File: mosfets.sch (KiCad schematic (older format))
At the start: 28 parts, among them Q12 PSMN1R2-30YLC,115, Q13 PSMN1R2-30YLC,115, Q14 PSMN1R2-30YLC,115, Q15 IRLML0030TRPbF, Q16 IRLML0030TRPbF, Q17 IRLML0030TRPbF, Q18 IRLML0030TRPbF

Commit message: Improve Readability
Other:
- moved on the sheet: D10, D11, D12, D13, D7, D8, D9, R39, R43
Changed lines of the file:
@@
 L Device:D_Schottky D7
 U 1 1 5B1A3271
-P 1950 1300
-F 0 "D7" H 1950 1516 50  0000 C CNN
-F 1 "SK310A-LTP" H 1950 1425 50  0000 C CNN
-F 2 "Diode_SMD:D_SMA" H 1950 1300 50  0001 C CNN
-F 3 "https://www.mouser.de/ProductDetail/Micro-Commercial-Components-MCC/SK310A-TP?qs=O2qRfqcg9D9SKx4%252bV6P4XQ%3D%3D" H 1950 1300 50  0001 C CNN
-	1    1950 1300
-	1    0    0    -1
-$EndComp
-Wire Wire Line
-	1700 1300 1800 1300
+P 2000 1300
+F 0 "D7" H 2000 1516 50  0000 C CNN
+F 1 "SK310A-LTP" H 2000 1425 50  0000 C CNN
+F 2 "Diode_SMD:D_SMA" H 2000 1300 50  0001 C CNN
+F 3 "https://www.mouser.de/ProductDetail/Micro-Commercial-Components-MCC/SK310A-TP?qs=O2qRfqcg9D9SKx4%252bV6P4XQ%3D%3D" H 2000 1300 50  0001 C CNN
+	1    2000 1300
+	1    0    0    -1
+$EndComp
+Wire Wire Line
+	1700 1300 1850 1300
 $Comp
 L heteromycin:PSMN1R8-40YLC,115 Q12
@@
 L Device:D_Schottky D8
 U 1 1 5B1B03B6
-P 1950 2950
-F 0 "D8" H 1950 3166 50  0000 C CNN
-F 1 "SK310A-LTP" H 1950 3075 50  0000 C CNN
-F 2 "Diode_SMD:D_SMA" H 1950 2950 50  0001 C CNN
-F 3 "https://www.mouser.de/ProductDetail/Micro-Commercial-Components-MCC/SK310A-TP?qs=O2qRfqcg9D9SKx4%252bV6P4XQ%3D%3D" H 1950 2950 50  0001 C CNN
-	1    1950 2950
-	1    0    0    -1
-$EndComp
-Wire Wire Line
-	1700 2950 1800 2950
+P 2000 2950
+F 0 "D8" H 2000 3166 50  0000 C CNN
+F 1 "SK310A-LTP" H 2000 3075 50  0000 C CNN
+F 2 "Diode_SMD:D_SMA" H 2000 2950 50  0001 C CNN
+F 3 "https://www.mouser.de/ProductDetail/Micro-Commercial-Components-MCC/SK310A-TP?qs=O2qRfqcg9D9SKx4%252bV6P4XQ%3D%3D" H 2000 2950 50  0001 C CNN
+	1    2000 2950
+	1    0    0    -1
+$EndComp
+Wire Wire Line
+	1700 2950 1850 2950
 Wire Wire Line
 	2400 3850 2500 3850
@@
 	2300 3200 2300 2950
 Wire Wire Line
-	2300 2950 2100 2950
-Wire Wire Line
-	2100 1300 2300 1300
+	2300 2950 2150 2950
+Wire Wire Line
+	2150 1300 2300 1300
 Connection ~ 2300 1300
 Wire Wire Line
@@
 	4900 1750 5000 1750
 Wire Wire Line
-	5250 1300 5350 1300
-Wire Wire Line
-	5650 1300 5850 1300
+	5250 1300 5400 1300
+Wire Wire Line
+	5700 1300 5850 1300
 Connection ~ 5850 1300
 Wire Wire Line
@@
 L Device:R R39
 U 1 1 5B2008D0
-P 5150 3400
-F 0 "R39" V 4943 3400 50  0000 C CNN
-F 1 "100" V 5034 3400 50  0000 C CNN
-F 2 "Resistor_SMD:R_0603_1608Metric" V 5080 3400 50  0001 C CNN
-F 3 "~" H 5150 3400 50  0001 C CNN
-	1    5150 3400
-	0    1    1    0
-$EndComp
-Text HLabel 4900 3400 0    50   Input ~ 0
+P 5200 3400
+F 0 "R39" V 4993 3400 50  0000 C CNN
+F 1 "100" V 5084 3400 50  0000 C CNN
+F 2 "Resistor_SMD:R_0603_1608Metric" V 5130 3400 50  0001 C CNN
+F 3 "~" H 5200 3400 50  0001 C CNN
+	1    5200 3400
+	0    1    1    0
+$EndComp
+Text HLabel 4950 3400 0    50   Input ~ 0
 PWM_FAN3
 Wire Wire Line
-	4900 3400 5000 3400
-Wire Wire Line
-	5250 2950 5350 2950
-Wire Wire Line
-	5650 2950 5850 2950
+	4950 3400 5050 3400
+Wire Wire Line
+	5250 2950 5400 2950
+Wire Wire Line
+	5700 2950 5850 2950
 Connection ~ 5850 2950
 Wire Wire Line
@@
 Wire Wire Line
 	5350 1750 5550 1750
-Wire Wire Line
-	1650 1750 1800 1750
-Wire Wire Line
-	1650 3400 1800 3400
 $Comp
 L Device:R R35
@@
 	2300 2200 2100 2200
 Connection ~ 2300 2200
-Wire Wire Line
-	1800 2200 1800 1750
-Connection ~ 1800 1750
-Wire Wire Line
-	1800 1750 2000 1750
 $Comp
 L Device:R R36
@@
 Wire Wire Line
 	5400 3850 5500 3850
-Wire Wire Line
-	5300 3400 5400 3400
 Connection ~ 5400 3400
 Wire Wire Line
@@
 	5850 3850 5800 3850
 Connection ~ 5850 3850
-Wire Wire Line
-	1800 3850 1800 3400
-Connection ~ 1800 3400
-Wire Wire Line
-	1800 3400 2000 3400
 Text GLabel 5250 1300 0    50   Input ~ 0
 VDD_FAN
@@
 L Device:D_Schottky D10
 U 1 1 5BD6B250
-P 5500 1300
-F 0 "D10" H 5450 1500 50  0000 L CNN
-F 1 "BAT54GWJ" H 5300 1400 50  0000 L CNN
-F 2 "Diode_SMD:D_SOD-123" H 5500 1300 50  0001 C CNN
-F 3 "https://www.mouser.de/datasheet/2/916/BAT54GW-1318921.pdf" H 5500 1300 50  0001 C CNN
-	1    5500 1300
+P 5550 1300
+F 0 "D10" H 5500 1500 50  0000 L CNN
+F 1 "BAT54GWJ" H 5350 1400 50  0000 L CNN
+F 2 "Diode_SMD:D_SOD-123" H 5550 1300 50  0001 C CNN
+F 3 "https://www.mouser.de/datasheet/2/916/BAT54GW-1318921.pdf" H 5550 1300 50  0001 C CNN
+	1    5550 1300
 	1    0    0    -1
 $EndComp
@@
 L Device:D_Schottky D11
 U 1 1 5BD6D4A2
-P 5500 2950
-F 0 "D11" H 5450 3150 50  0000 L CNN
-F 1 "BAT54GWJ" H 5300 3050 50  0000 L CNN
-F 2 "Diode_SMD:D_SOD-123" H 5500 2950 50  0001 C CNN
-F 3 "https://www.mouser.de/datasheet/2/916/BAT54GW-1318921.pdf" H 5500 2950 50  0001 C CNN
-	1    5500 2950
+P 5550 2950
+F 0 "D11" H 5500 3150 50  0000 L CNN
+F 1 "BAT54GWJ" H 5350 3050 50  0000 L CNN
+F 2 "Diode_SMD:D_SOD-123" H 5550 2950 50  0001 C CNN
+F 3 "https://www.mouser.de/datasheet/2/916/BAT54GW-1318921.pdf" H 5550 2950 50  0001 C CNN
+	1    5550 2950
 	1    0    0    -1
 $EndComp
@@
 L Device:D_Schottky D9
 U 1 1 5BC4CDE5
-P 1950 4450
-F 0 "D9" H 1950 4666 50  0000 C CNN
-F 1 "SK310A-LTP" H 1950 4575 50  0000 C CNN
-F 2 "Diode_SMD:D_SMA" H 1950 4450 50  0001 C CNN
-F 3 "https://www.mouser.de/ProductDetail/Micro-Commercial-Components-MCC/SK310A-TP?qs=O2qRfqcg9D9SKx4%252bV6P4XQ%3D%3D" H 1950 4450 50  0001 C CNN
-	1    1950 4450
-	1    0    0    -1
-$EndComp
-Wire Wire Line
-	1700 4450 1800 4450
+P 2000 4450
+F 0 "D9" H 2000 4666 50  0000 C CNN
+F 1 "SK310A-LTP" H 2000 4575 50  0000 C CNN
+F 2 "Diode_SMD:D_SMA" H 2000 4450 50  0001 C CNN
+F 3 "https://www.mouser.de/ProductDetail/Micro-Commercial-Components-MCC/SK310A-TP?qs=O2qRfqcg9D9SKx4%252bV6P4XQ%3D%3D" H 2000 4450 50  0001 C CNN
+	1    2000 4450
+	1    0    0    -1
+$EndComp
+Wire Wire Line
+	1700 4450 1850 4450
 Wire Wire Line
 	2400 5350 2500 5350
@@
 	2300 4700 2300 4450
 Wire Wire Line
-	2300 4450 2100 4450
+	2300 4450 2150 4450
 Wire Wire Line
 	2600 4450 2300 4450
 Connection ~ 2300 4450
-Wire Wire Line
-	1650 4900 1800 4900
 $Comp
 L Device:R R37
@@
 Wire Wire Line
 	2300 5350 2100 5350
-Wire Wire Line
-	1800 5350 1800 4900
-Connection ~ 1800 4900
-Wire Wire Line
-	1800 4900 2000 4900
 $Comp
 L heteromycin:PSMN1R8-40YLC,115 Q14
@@
 	7350 1750 7450 1750
 Wire Wire Line
-	7700 1300 7800 1300
-Wire Wire Line
-	8100 1300 8300 1300
+	7700 1300 7850 1300
+Wire Wire Line
+	8150 1300 8300 1300
 Connection ~ 8300 1300
 Wire Wire Line
@@
 L Device:R R43
 U 1 1 5BC57CE1
-P 7600 3400
-F 0 "R43" V 7393 3400 50  0000 C CNN
-F 1 "100" V 7484 3400 50  0000 C CNN
-F 2 "Resistor_SMD:R_0603_1608Metric" V 7530 3400 50  0001 C CNN
-F 3 "~" H 7600 3400 50  0001 C CNN
-	1    7600 3400
-	0    1    1    0
-$EndComp
-Text HLabel 7350 3400 0    50   Input ~ 0
+P 7650 3400
+F 0 "R43" V 7443 3400 50  0000 C CNN
+F 1 "100" V 7534 3400 50  0000 C CNN
+F 2 "Resistor_SMD:R_0603_1608Metric" V 7580 3400 50  0001 C CNN
+F 3 "~" H 7650 3400 50  0001 C CNN
+	1    7650 3400
+	0    1    1    0
+$EndComp
+Text HLabel 7400 3400 0    50   Input ~ 0
 PWM_FAN4
 Wire Wire Line
-	7350 3400 7450 3400
-Wire Wire Line
-	7700 2950 7800 2950
-Wire Wire Line
-	8100 2950 8300 2950
+	7400 3400 7500 3400
+Wire Wire Line
+	7700 2950 7850 2950
+Wire Wire Line
+	8150 2950 8300 2950
 Connection ~ 8300 2950
 Wire Wire Line
@@
 	7850 3850 7950 3850
 Wire Wire Line
-	7750 3400 7850 3400
+	7800 3400 7850 3400
 Connection ~ 7850 3400
-Wire Wire Line
-	7850 3400 8000 3400
 Wire Wire Line
 	8300 3850 8250 3850
@@
 L Device:D_Schottky D12
 U 1 1 5BC57D0F
-P 7950 1300
-F 0 "D12" H 7900 1500 50  0000 L CNN
-F 1 "BAT54GWJ" H 7750 1400 50  0000 L CNN
-F 2 "Diode_SMD:D_SOD-123" H 7950 1300 50  0001 C CNN
-F 3 "https://www.mouser.de/datasheet/2/916/BAT54GW-1318921.pdf" H 7950 1300 50  0001 C CNN
-	1    7950 1300
+P 8000 1300
+F 0 "D12" H 7950 1500 50  0000 L CNN
+F 1 "BAT54GWJ" H 7800 1400 50  0000 L CNN
+F 2 "Diode_SMD:D_SOD-123" H 8000 1300 50  0001 C CNN
+F 3 "https://www.mouser.de/datasheet/2/916/BAT54GW-1318921.pdf" H 8000 1300 50  0001 C CNN
+	1    8000 1300
 	1    0    0    -1
 $EndComp
@@
 L Device:D_Schottky D13
 U 1 1 5BC57D16
-P 7950 2950
-F 0 "D13" H 7900 3150 50  0000 L CNN
-F 1 "BAT54GWJ" H 7750 3050 50  0000 L CNN
-F 2 "Diode_SMD:D_SOD-123" H 7950 2950 50  0001 C CNN
-F 3 "https://www.mouser.de/datasheet/2/916/BAT54GW-1318921.pdf" H 7950 2950 50  0001 C CNN
-	1    7950 2950
+P 8000 2950
+F 0 "D13" H 7950 3150 50  0000 L CNN
+F 1 "BAT54GWJ" H 7800 3050 50  0000 L CNN
+F 2 "Diode_SMD:D_SOD-123" H 8000 2950 50  0001 C CNN
+F 3 "https://www.mouser.de/datasheet/2/916/BAT54GW-1318921.pdf" H 8000 2950 50  0001 C CNN
+	1    8000 2950
 	1    0    0    -1
 $EndComp
@@
 	1    0    0    -1
 $EndComp
+Wire Wire Line
+	7850 3400 8000 3400
+Wire Wire Line
+	5350 3400 5400 3400
+Wire Wire Line
+	1650 1750 1750 1750
+Wire Wire Line
+	1800 2200 1750 2200
+Wire Wire Line
+	1750 2200 1750 1750
+Connection ~ 1750 1750
+Wire Wire Line
+	1750 1750 2000 1750
+Wire Wire Line
+	1650 3400 1750 3400
+Wire Wire Line
+	1800 3850 1750 3850
+Wire Wire Line
+	1750 3850 1750 3400
+Connection ~ 1750 3400
+Wire Wire Line
+	1750 3400 2000 3400
+Wire Wire Line
+	1650 4900 1750 4900
+Wire Wire Line
+	1800 5350 1750 5350
+Wire Wire Line
+	1750 5350 1750 4900
+Connection ~ 1750 4900
+Wire Wire Line
+	1750 4900 2000 4900
 $EndSCHEMATC

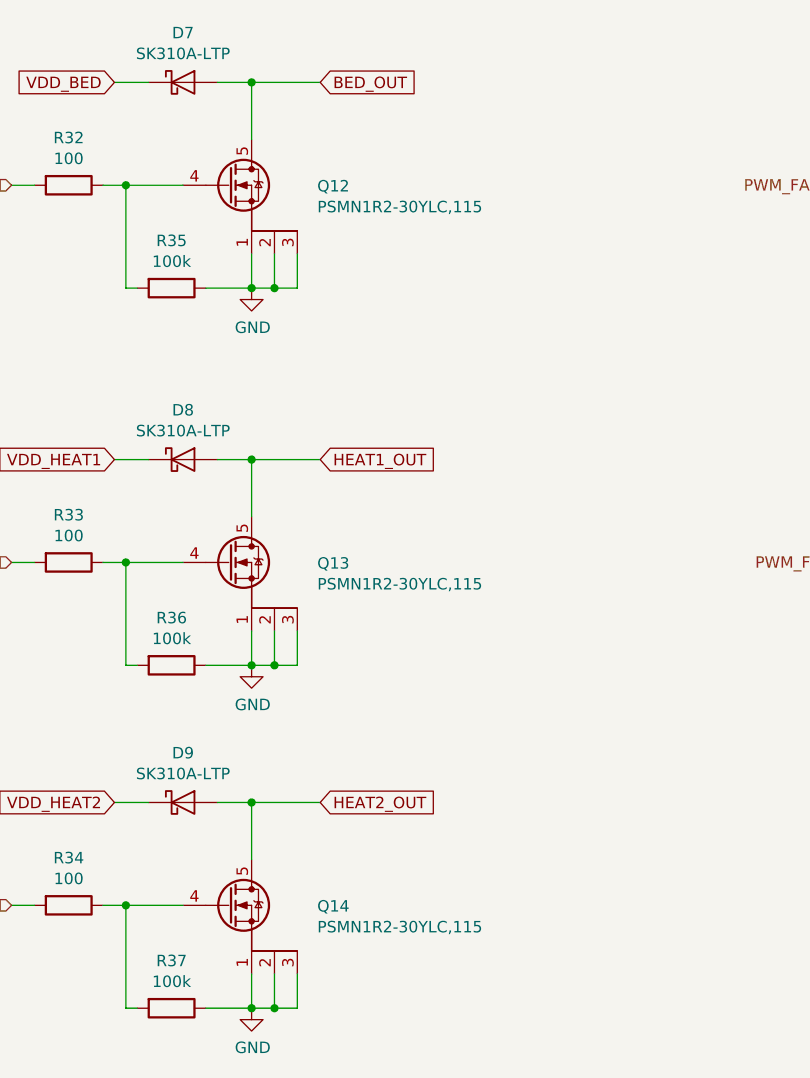
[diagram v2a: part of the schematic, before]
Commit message: Further Improved Readability - Rotated labels
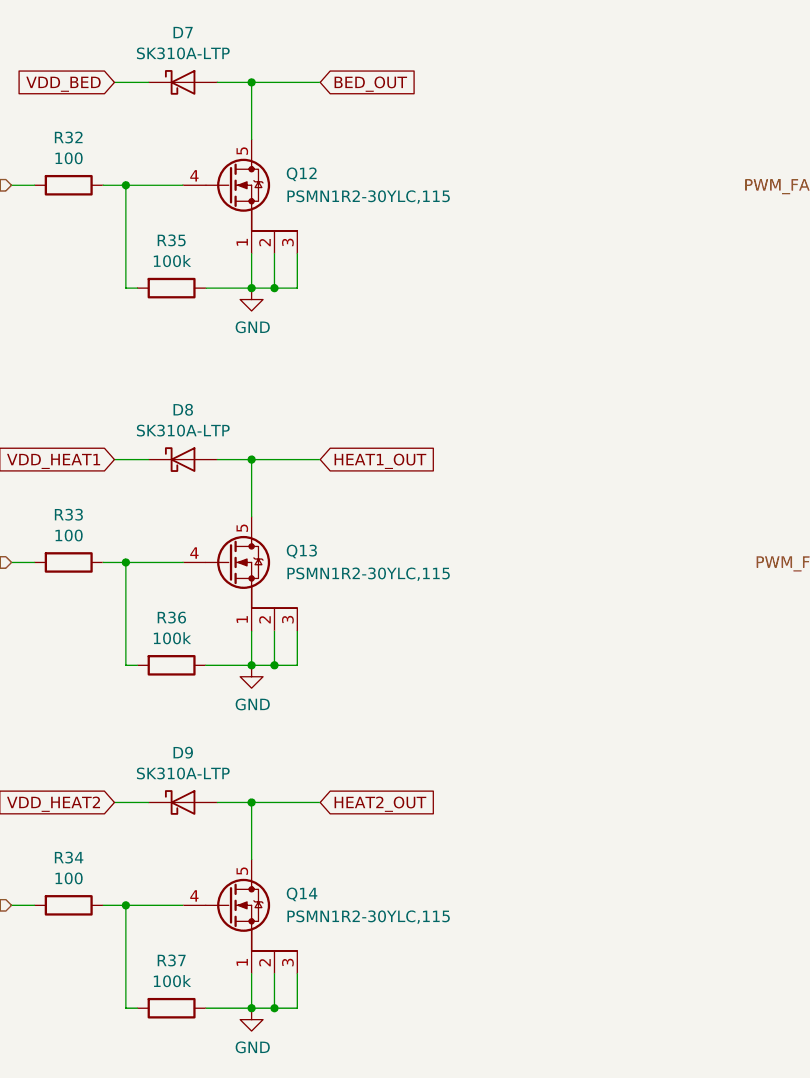
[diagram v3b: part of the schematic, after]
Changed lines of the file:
@@
 U 1 1 5B1A764D
 P 2200 1750
-F 0 "Q12" H 2587 1746 50  0000 L CNN
-F 1 "PSMN1R2-30YLC,115" H 2587 1655 50  0000 L CNN
+F 0 "Q12" H 2450 1800 50  0000 L CNN
+F 1 "PSMN1R2-30YLC,115" H 2450 1700 50  0000 L CNN
 F 2 "heteromycin:SOT-669_LFPAK_ThermalVias-1" H 2400 1675 50  0001 L CIN
 F 3 "https://assets.nexperia.com/documents/data-sheet/PSMN1R2-30YLC.pdf" V 2200 1750 50  0001 L CNN
@@
 U 1 1 5BC30682
 P 2200 3400
-F 0 "Q13" H 2587 3396 50  0000 L CNN
-F 1 "PSMN1R2-30YLC,115" H 2587 3305 50  0000 L CNN
+F 0 "Q13" H 2450 3450 50  0000 L CNN
+F 1 "PSMN1R2-30YLC,115" H 2450 3350 50  0000 L CNN
 F 2 "heteromycin:SOT-669_LFPAK_ThermalVias-1" H 2400 3325 50  0001 L CIN
 F 3 "https://assets.nexperia.com/documents/data-sheet/PSMN1R2-30YLC.pdf" V 2200 3400 50  0001 L CNN
@@
 U 1 1 5BC4CE0B
 P 2200 4900
-F 0 "Q14" H 2587 4896 50  0000 L CNN
-F 1 "PSMN1R2-30YLC,115" H 2587 4805 50  0000 L CNN
+F 0 "Q14" H 2450 4950 50  0000 L CNN
+F 1 "PSMN1R2-30YLC,115" H 2450 4850 50  0000 L CNN
 F 2 "heteromycin:SOT-669_LFPAK_ThermalVias-1" H 2400 4825 50  0001 L CIN
 F 3 "https://assets.nexperia.com/documents/data-sheet/PSMN1R2-30YLC.pdf" V 2200 4900 50  0001 L CNN
